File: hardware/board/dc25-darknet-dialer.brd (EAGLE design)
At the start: 101.6 x 101.6 mm, 61 parts

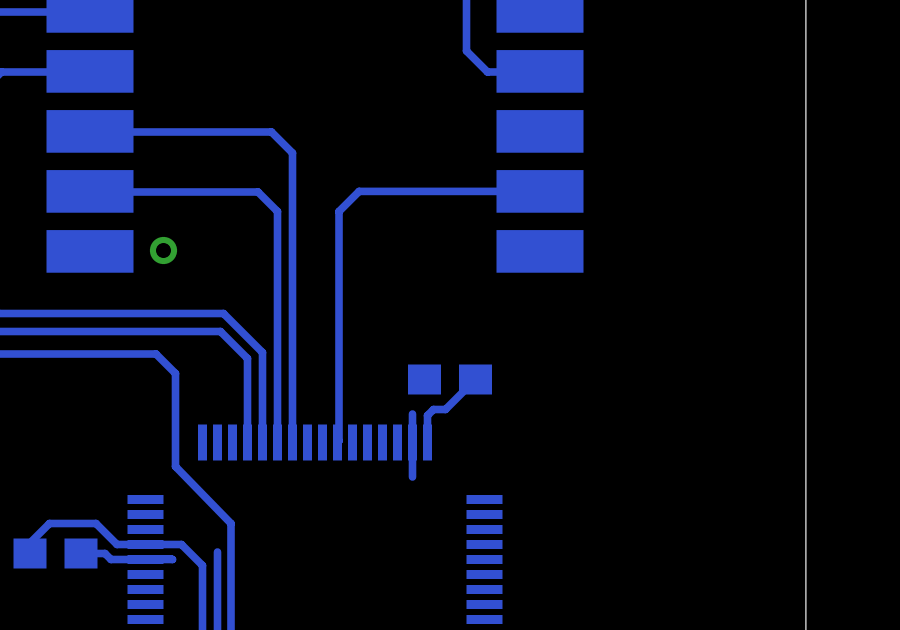
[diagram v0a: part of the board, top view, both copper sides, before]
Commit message: Updated board to include values for bypass caps
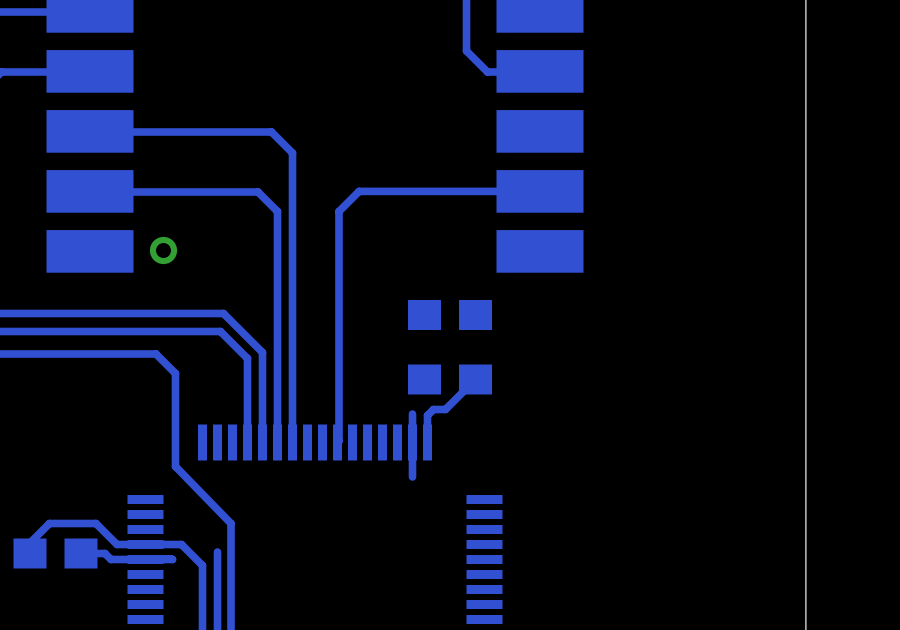
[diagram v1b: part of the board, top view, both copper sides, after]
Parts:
- added C16: 4.7uF, SYNShop:C0603
- C12, C13, C14: value (none) -> 100nF
- C15: value (none) -> 10nF
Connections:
- net GND: now also C16.1
- net VCC: now also C16.2
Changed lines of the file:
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@@
 <element name="C11" library="SYNShop" package="C0603" value="" x="78.74" y="44.45" rot="MR0"/>
 <element name="U$2" library="darknet_parts_library" package="LQFP64" value="STM32F302XC" x="50.8" y="39.4" rot="MR180"/>
-<element name="C12" library="SYNShop" package="C0603" value="" x="46.4" y="31.7" rot="MR0"/>
-<element name="C13" library="SYNShop" package="C0603" value="" x="58.5" y="34.9" rot="MR270"/>
-<element name="C14" library="SYNShop" package="C0603" value="" x="55.3" y="47.15" rot="MR180"/>
-<element name="C15" library="SYNShop" package="C0603" value="" x="42.15" y="41.35" rot="MR0"/>
+<element name="C12" library="SYNShop" package="C0603" value="100nF" x="46.4" y="31.7" rot="MR0"/>
+<element name="C13" library="SYNShop" package="C0603" value="100nF" x="58.5" y="34.9" rot="MR270"/>
+<element name="C14" library="SYNShop" package="C0603" value="100nF" x="55.3" y="47.15" rot="MR180"/>
+<element name="C15" library="SYNShop" package="C0603" value="10nF" x="42.15" y="41.35" rot="MR0"/>
+<element name="C16" library="SYNShop" package="C0603" value="4.7uF" x="55.3" y="49.3" rot="MR180"/>
 </elements>
 <signals>
@@
 <wire x1="43" y1="41.35" x2="43.8" y2="41.35" width="0.254" layer="16"/>
 <wire x1="43.8" y1="41.35" x2="44" y2="41.15" width="0.254" layer="16"/>
+<contactref element="C16" pad="1"/>
+<wire x1="79.59" y1="66.04" x2="81.788" y2="70.612" width="0" layer="19" extent="16-16"/>
+<wire x1="64.008" y1="80.772" x2="76.2" y2="78.462" width="0" layer="19" extent="16-16"/>
+<wire x1="61.81" y1="76.2" x2="64.008" y2="80.772" width="0" layer="19" extent="16-16"/>
+<wire x1="57.15" y1="71.12" x2="61.81" y2="76.2" width="0" layer="19" extent="16-16"/>
+<wire x1="58.3" y1="63.42" x2="57.15" y2="71.12" width="0" layer="19" extent="16-16"/>
+<wire x1="43.3" y1="65.42" x2="57.15" y2="71.12" width="0" layer="19" extent="16-16"/>
+<wire x1="41.49" y1="76.2" x2="43.3" y2="65.42" width="0" layer="19" extent="16-16"/>
+<wire x1="43.688" y1="80.772" x2="41.49" y2="76.2" width="0" layer="19" extent="16-16"/>
+<wire x1="43.3" y1="51.42" x2="43.3" y2="65.42" width="0" layer="19" extent="16-16"/>
+<wire x1="45.75" y1="51.45" x2="43.3" y2="51.42" width="0" layer="19" extent="16-16"/>
+<wire x1="54.45" y1="47.15" x2="45.75" y2="51.45" width="0" layer="19" extent="16-16"/>
+<wire x1="54.05" y1="46" x2="54.45" y2="47.15" width="0" layer="19" extent="16-16"/>
+<wire x1="47.55" y1="41.4" x2="54.05" y2="43.9" width="0" layer="19" extent="16-16"/>
+<wire x1="46.05" y1="41.15" x2="47.55" y2="41.4" width="0" layer="19" extent="16-16"/>
+<wire x1="55.45" y1="36.15" x2="54.05" y2="43.9" width="0" layer="19" extent="16-16"/>
+<wire x1="58.5" y1="35.75" x2="57.5" y2="36.17" width="0" layer="19" extent="16-16"/>
+<wire x1="41.49" y1="22.86" x2="47.25" y2="31.7" width="0" layer="19" extent="16-16"/>
+<wire x1="43.434" y1="20.828" x2="41.49" y2="22.86" width="0" layer="19" extent="16-16"/>
+<wire x1="61.81" y1="22.86" x2="58.5" y2="35.75" width="0" layer="19" extent="16-16"/>
+<wire x1="64.008" y1="20.574" x2="61.81" y2="22.86" width="0" layer="19" extent="16-16"/>
+<wire x1="73.406" y1="26.162" x2="64.008" y2="20.574" width="0" layer="19" extent="16-16"/>
+<wire x1="78.32" y1="33.02" x2="73.406" y2="29.972" width="0" layer="19" extent="16-16"/>
+<wire x1="79.59" y1="44.45" x2="78.32" y2="33.02" width="0" layer="19" extent="16-16"/>
+<wire x1="27.178" y1="76.2" x2="41.49" y2="76.2" width="0" layer="19" extent="16-16"/>
+<wire x1="24.98" y1="66.04" x2="27.178" y2="71.12" width="0" layer="19" extent="16-16"/>
+<wire x1="21.082" y1="63.246" x2="24.98" y2="66.04" width="0" layer="19" extent="16-16"/>
+<wire x1="24.98" y1="58.42" x2="21.082" y2="63.246" width="0" layer="19" extent="16-16"/>
+<wire x1="20.828" y1="43.18" x2="24.98" y2="58.42" width="0" layer="19" extent="16-16"/>
 <wire x1="23.71" y1="38.1" x2="20.828" y2="43.18" width="0" layer="19" extent="16-16"/>
+<wire x1="23.71" y1="33.02" x2="23.71" y2="38.1" width="0" layer="19" extent="16-16"/>
+<wire x1="25.908" y1="30.988" x2="23.71" y2="33.02" width="0" layer="19" extent="16-16"/>
+<wire x1="54.45" y1="49.3" x2="20.828" y2="23.344" width="0" layer="19" extent="1-16"/>
 </signal>
 <signal name="N$1">
@@
 <wire x1="46.85" y1="32.7" x2="46.55" y2="32.7" width="0.254" layer="16"/>
 <wire x1="46.55" y1="32.7" x2="45.55" y2="31.7" width="0.254" layer="16"/>
+<contactref element="C16" pad="2"/>
 <wire x1="56.15" y1="47.15" x2="56.55" y2="57.4" width="0" layer="19" extent="16-16"/>
 <wire x1="48.05" y1="45.05" x2="54.55" y2="45.05" width="0" layer="19" extent="16-16"/>
 <wire x1="46.35" y1="41.65" x2="48.05" y2="45.05" width="0" layer="19" extent="16-16"/>
 <wire x1="56.45" y1="35.65" x2="54.55" y2="45.05" width="0" layer="19" extent="16-16"/>
+<wire x1="56.15" y1="49.3" x2="45.55" y2="31.7" width="0" layer="19" extent="1-16"/>
 </signal>
 </signals>

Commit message: Routing and layout progress
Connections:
- net N$38 renamed OLED_SPI_NSS
- new net N$38: U$2.P5
- new net N$39: U$2.P6
- new net N$40: U$2.P2
- new net N$41: U$2.P61
- new net N$42: U$2.P60
- new net N$43: U$2.P57
- new net N$44: U$2.P54
- new net N$45: U$2.P53
- new net N$46: U$2.P52
- new net N$47: U$2.P51
- new net N$48: U$2.P50
- new net N$49: U$2.P41
- new net N$50: U$2.P40
- new net N$51: U$2.P39
- new net N$52: U$2.P38
- new net N$53: U$2.P37
- new net N$54: U$2.P3
- new net N$55: U$2.P4
- new net N$56: U$2.P1
- new net N$57: U$2.P8
- new net N$58: U$2.P9
- new net N$59: U$2.P10
- new net N$60: U$2.P11
- new net N$61: U$2.P29
- new net N$62: U$12.LED
- new net N$66: U$12.A0
- new net N$67: U$12.RESET
- new net OLED_SPI_MISO: U$2.P35
- new net OLED_SPI_MOSI: U$12.SDA, U$2.P36
- new net OLED_SPI_SCK: U$12.SCK, U$2.P34
- new net PB0: U$2.P26
- new net PB9: U$2.P62
- net RFM69_RESET: now also U$2.P18; no longer U$2.P62
- net RMF69_INTERRUPT_DIO0: now also U$2.P24; no longer U$2.P26
- net VCC: now also U$12.CS
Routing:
- net OLED_SPI_SCK: track 0.00 -> 36.1 mm, vias 0 -> 1
- net OLED_SPI_MOSI: track 0.00 -> 35.3 mm, vias 0 -> 1
- net VCC: track 41.3 -> 60.7 mm
- net RFM69_RESET: track 39.6 -> 29.0 mm
- net RMF69_INTERRUPT_DIO0: track 14.7 -> 15.7 mm

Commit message: Updated design
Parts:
- moved C15 3.25 mm to (42.1, 38.1)
- moved C12 2.65 mm to (46.4, 29.1)
- moved C13 2.65 mm to (58.5, 32.2)
- moved C14 2.65 mm to (55.3, 44.5)
- moved C16 2.65 mm to (55.3, 46.6)
- moved U$2 2.65 mm to (50.8, 36.8)
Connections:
- net N$28 renamed TSC_G3_IO4
- net N$31 renamed SYS_JTMS_SWDIO
- net N$32 renamed SYS_JTCK-SWCLK
- net N$38 renamed RCC_OSC_IN
- net N$39 renamed RCC_OSC_OUT
- net N$40 renamed LED_STATUS
- net N$41 renamed TIM_IR_MAIN_SIGNAL
- net N$42 renamed BOOT0
- net PB9 renamed IR_OUT
- removed net N$22: U$2.P14
- removed net N$23: U$2.P15
- removed net N$24: U$2.P16
- removed net N$25: U$2.P17
- removed net N$26: U$2.P25
- removed net N$27: U$2.P27
- removed net N$33: U$2.P55
- removed net N$34: U$2.P56
- removed net N$35: U$2.P58
- removed net N$36: U$2.P59
- removed net PB0: U$2.P26
- removed net TOUCH0: R20.1
- removed net TOUCH1: R11.1
- removed net TOUCH2: R12.1
- removed net TOUCH3: R13.1
- removed net TOUCH4: R14.1
- removed net TOUCH5: R15.1
- removed net TOUCH6: R16.1
- removed net TOUCH7: R17.1
- removed net TOUCH8: R18.1
- removed net TOUCH9: R19.1
- removed net TOUCHHOOK: R21.1
- new net TSC_G1_IO1: R17.1, U$2.P14
- new net TSC_G1_IO2: R16.1, U$2.P15
- new net TSC_G1_IO3: R15.1, U$2.P16
- new net TSC_G1_IO4: R14.1, U$2.P17
- new net TSC_G3_IO1: R13.1, U$2.P25
- new net TSC_G3_IO2: R12.1, U$2.P26
- new net TSC_G3_IO3: R11.1, U$2.P27
- new net TSC_G5_IO1: R21.1, U$2.P55
- new net TSC_G5_IO2: R20.1, U$2.P56
- new net TSC_G5_IO3: R19.1, U$2.P58
- new net TSC_G5_IO4: R18.1, U$2.P59
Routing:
- net TSC_G3_IO1: track 0.00 -> 66.6 mm
- net TSC_G3_IO3: track 0.00 -> 51.9 mm
- net TSC_G3_IO2: track 0.00 -> 48.5 mm
- net TSC_G5_IO1: track 0.00 -> 45.1 mm
- net TSC_G1_IO4: track 0.00 -> 44.0 mm
- net TSC_G5_IO2: track 0.00 -> 37.7 mm
- net TSC_G1_IO3: track 0.00 -> 34.0 mm
- net VCC: track 60.7 -> 89.6 mm, vias 0 -> 5
- net TSC_G1_IO2: track 0.00 -> 23.2 mm
- net TSC_G1_IO1: track 0.00 -> 23.1 mm
- net TSC_G5_IO3: track 0.00 -> 16.6 mm
- net TSC_G5_IO4: track 0.00 -> 12.2 mm
- net GND: track 139.0 -> 146.6 mm
- net RMF69_INTERRUPT_DIO0: track 15.7 -> 18.4 mm
- net RFM69_SPI_SCK: track 24.0 -> 26.7 mm
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
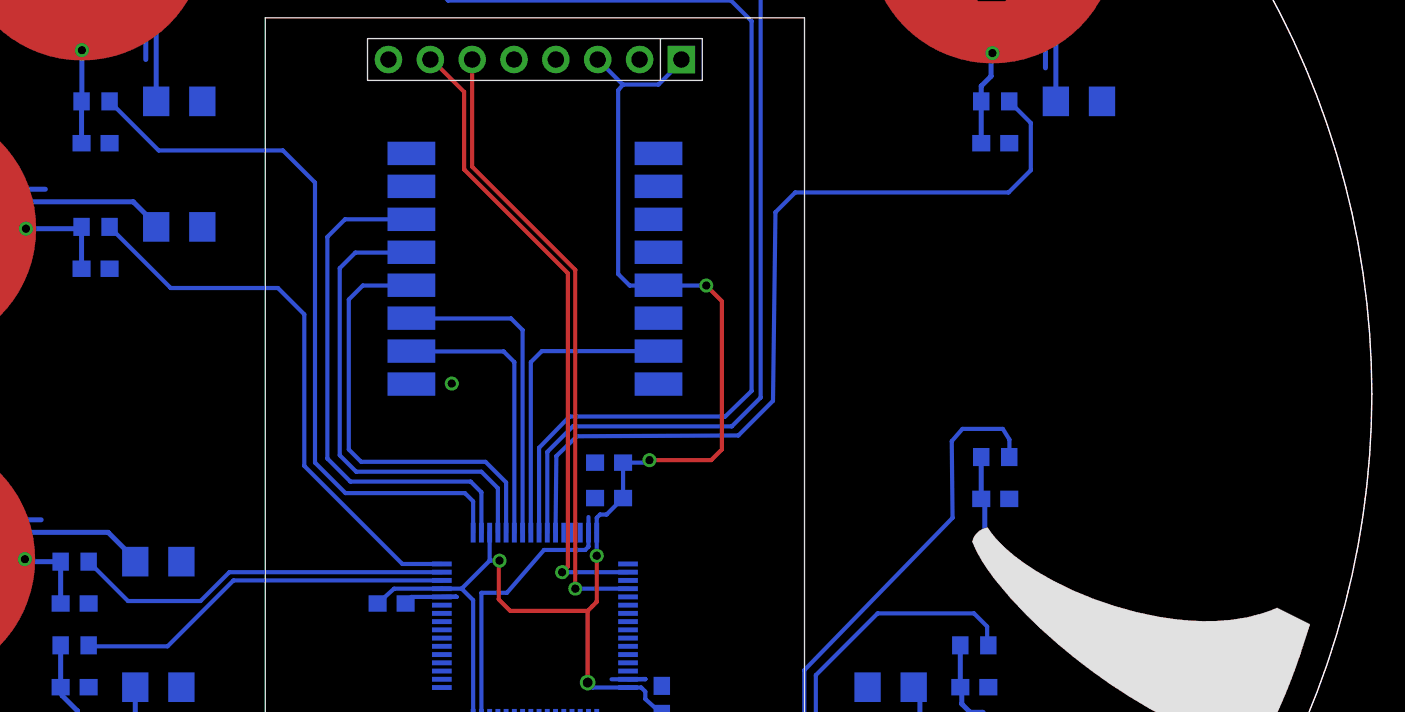
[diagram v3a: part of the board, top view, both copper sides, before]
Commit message: Added power and IR
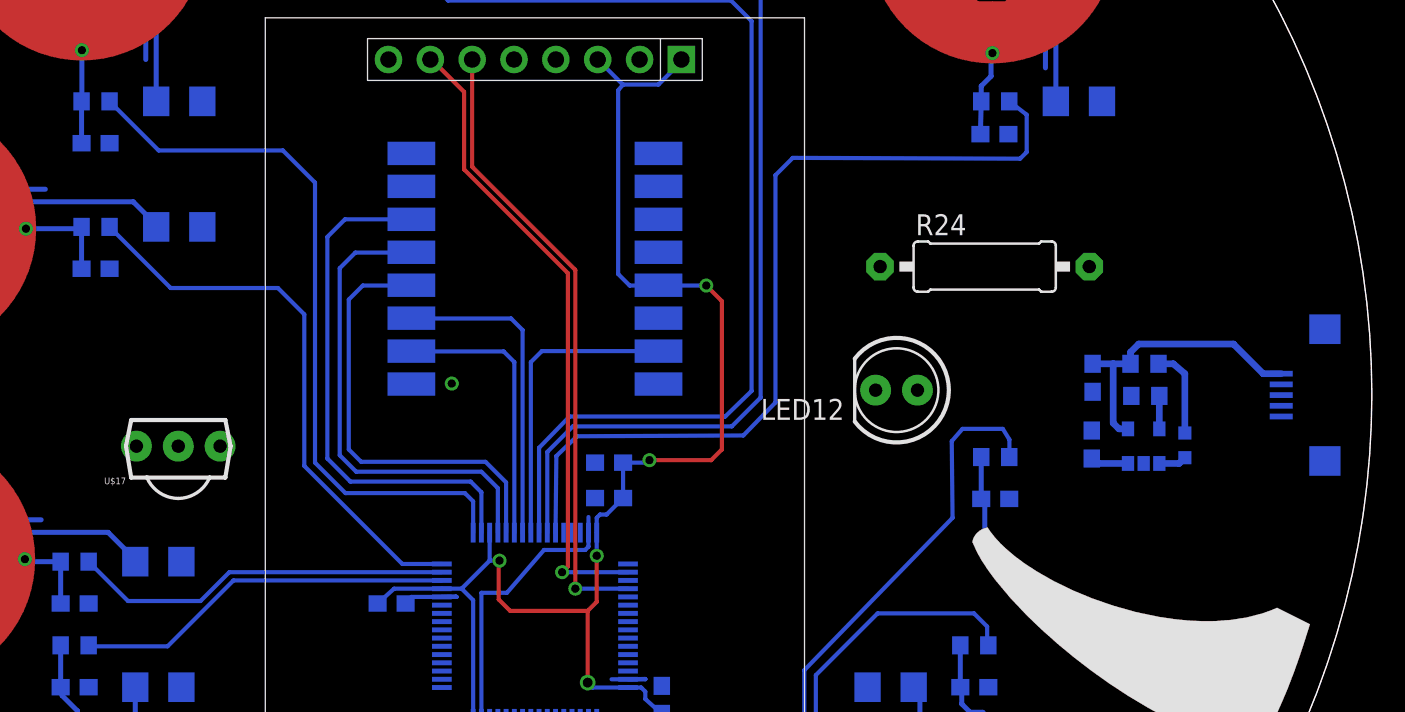
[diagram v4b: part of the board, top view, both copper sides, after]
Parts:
- added C17, C18: (no value), SYNShop:C0603
- added LED11: (no value), SYNShop:LED-0603
- added LED12: (no value), SYNShop:LED5MM
- added R22, R23: (no value), SYNShop:R0603
- added R24: (no value), SYNShop:0309/12
- added U$11: DS21984E, darknet_parts_library:SOT23-5
- added U$17: SOP22, SYNShop:IR-MODULE
- added X1: USB-MICROB, SYNShop:USB-MICROB
- moved C1 0.55 mm to (78.7, 66.6)
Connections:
- new net N$22: R22.2, U$11.5
- new net N$23: LED12.A, R24.2
- new net N$24: LED11.A, R23.1
- new net N$25: LED11.C, U$11.1
- new net VCC0: C18.2, R23.2, U$11.4, X1.VBUS
- net GND: now also C17.1, C18.1, R22.1, U$11.2, U$17.3, X1.GND
- net IR_OUT: now also R24.1
- net N$57: now also U$17.1
- net TIM_IR_MAIN_SIGNAL: now also LED12.K
- net VCC: now also C17.2, U$11.3, U$17.2
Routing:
- net VCC0: track 0.00 -> 17.7 mm
- net N$24: track 0.00 -> 5.42 mm
- net VCC: track 89.6 -> 91.9 mm
- net N$22: track 0.00 -> 2.00 mm
- net N$25: track 0.00 -> 1.69 mm
- net TSC_G3_IO3: track 51.9 -> 52.5 mm
- net N$1: track 5.75 -> 5.20 mm

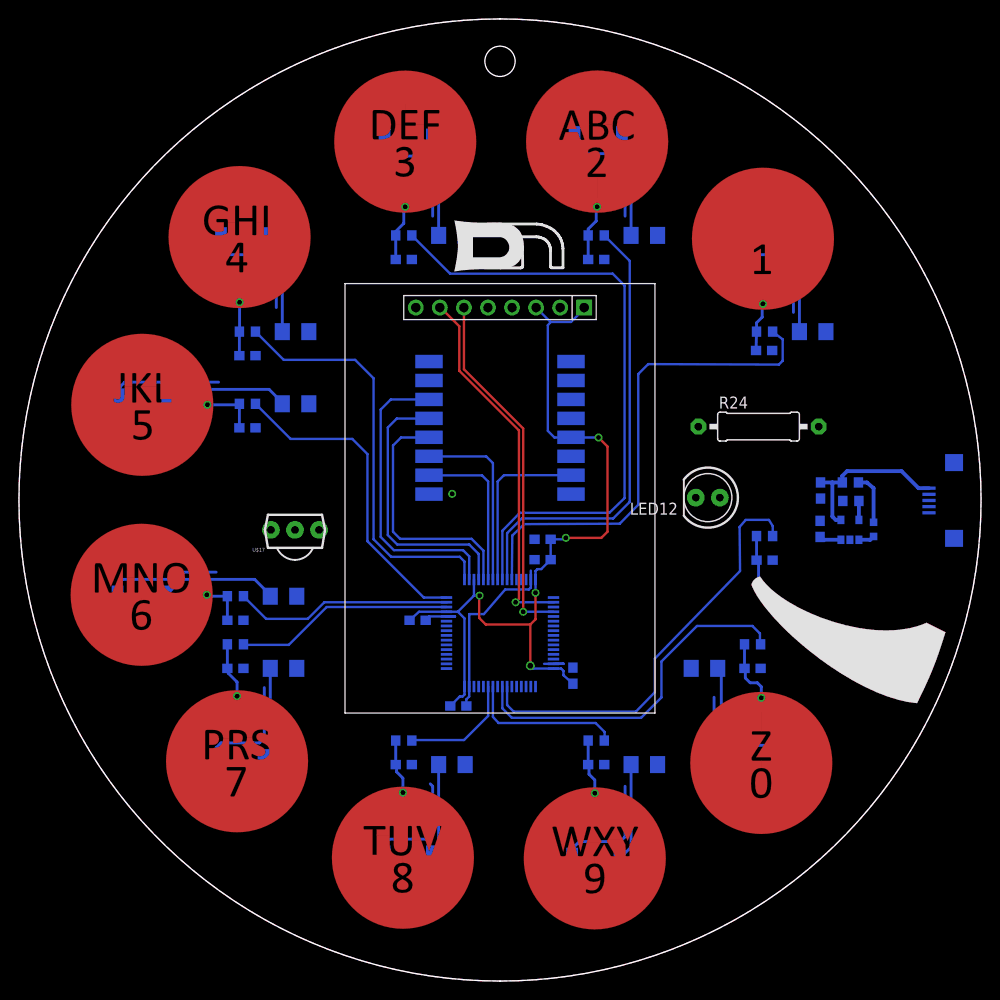
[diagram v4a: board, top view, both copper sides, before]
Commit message: Updated power, wired IR
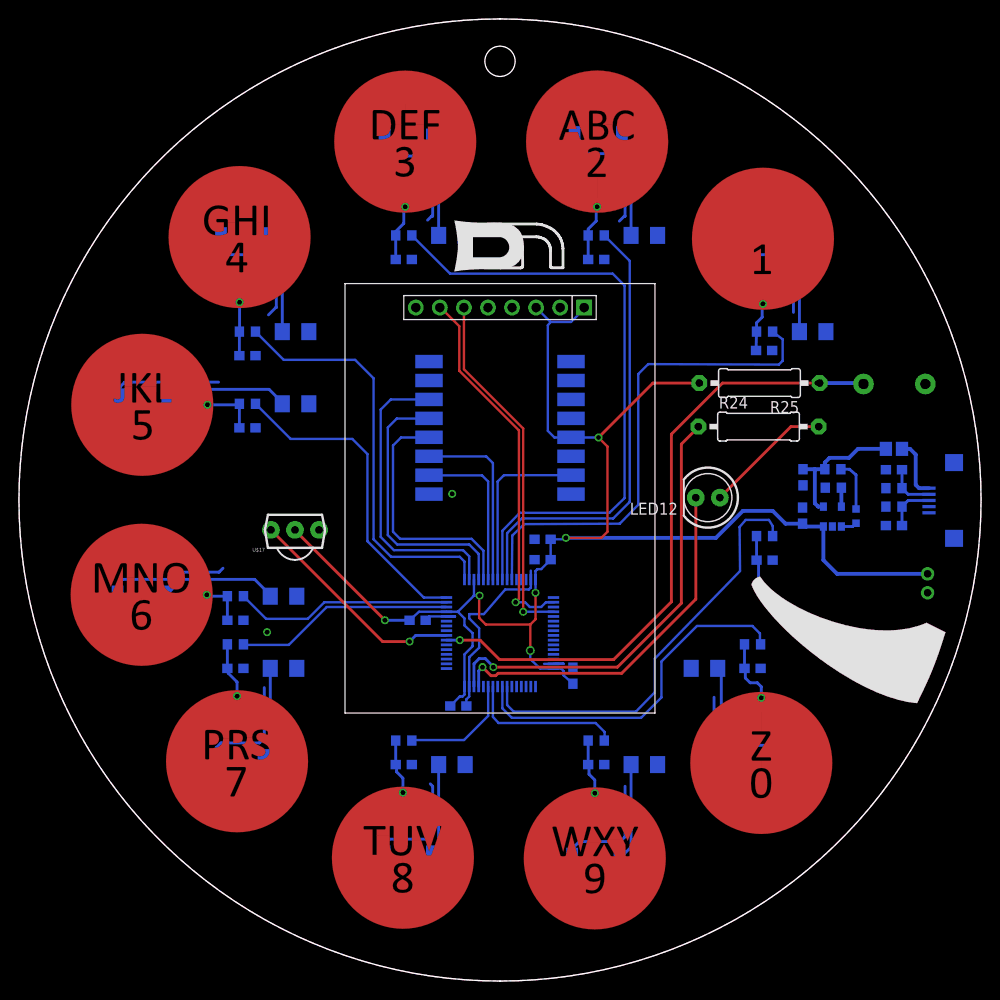
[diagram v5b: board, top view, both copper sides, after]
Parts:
- added C19, C20: (no value), SYNShop:C0603
- added CN1: (no value), adafruit:JST-PH-2-THM-RA
- added L1: (no value), dp_devices:FB603
- added R25: (no value), SYNShop:0309/12
- added R26, R27: (no value), SYNShop:R0603
- added SW1: RESET, SYNShop:TACTILE-2PIN-NARROW
- moved C18 2.32 mm to (82.8, 53.2)
- moved C17 2.32 mm to (82.8, 49.1)
- moved LED11 2.32 mm to (88.4, 49.1)
- moved R22 2.32 mm to (86.0, 52.1)
- moved R23 2.32 mm to (86.0, 54.0)
- moved U$11 2.32 mm to (85.9, 49.0)
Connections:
- new net N$26: C19.2, R27.1, X1.D+
- new net N$27: C20.2, R26.1, X1.D-
- new net N$28: L1.2, X1.VBUS
- net GND: now also C19.1, C20.1, CN1.1, SW1.P$2
- net RESET: now also R25.1, SW1.P$1
- net VCC: now also CN1.2, R25.2
- net VCC0: now also L1.1; no longer X1.VBUS
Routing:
- net VCC: track 91.9 -> 163.2 mm, vias 5 -> 6
- net RESET: track 0.00 -> 67.4 mm, vias 0 -> 2
- net IR_OUT: track 0.00 -> 47.1 mm, vias 0 -> 1
- net TIM_IR_MAIN_SIGNAL: track 0.00 -> 39.2 mm, vias 0 -> 1
- net N$57: track 0.00 -> 23.7 mm, vias 0 -> 1
- net N$23: track 0.00 -> 13.5 mm
- net N$28: track 0.00 -> 6.44 mm
- net N$26: track 0.00 -> 5.12 mm
- net N$27: track 0.00 -> 5.07 mm
- net GND: track 146.6 -> 151.1 mm, vias 1 -> 2
- net VCC0: track 17.7 -> 14.7 mm
